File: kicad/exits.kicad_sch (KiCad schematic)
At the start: 54 parts, among them J1 PJ301M12, J12 Euro power header, J13 PJ301M12, J14 PJ301M12, J2 PJ301M12, J3 PJ301M12, J4 PJ301M12, J5 Attenuator Jumper 1, J6 Attenuator Jumper 2, U1 TL074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

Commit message: note about pot taper
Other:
- note added: "Expect input signals to be 10Vpp (i.e +5V to -5V)"
- note added: "While most of the internet says we should use a log (A) pot for volume, I'm copying the Erica Synths Output, Exits, and the Befaco Hexmix, which all used a B10K for volume"
- note removed: "Expect inputs of 5Vpp"
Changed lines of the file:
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@@
     (effects (font (size 1.524 1.524)) (justify left bottom))
   )
-  (text "headphone volume" (at 71.755 156.845 90)
-    (effects (font (size 1.524 1.524)) (justify left bottom))
+  (text "headphone volume" (at 76.2 135.89 180)
+    (effects (font (size 1.524 1.524)) (justify right bottom))
   )
   (text "3.39hz highpass" (at 88.9 121.92 0)
@@
     (effects (font (size 1.524 1.524)) (justify left bottom))
   )
+  (text "While most of the internet says we should use a log (A) pot\nfor volume, I'm copying the Erica Synths Output, Exits,\nand the Befaco Hexmix, which all used a B10K for volume"
+    (at 13.335 152.4 0)
+    (effects (font (size 1.524 1.524)) (justify left bottom))
+  )
   (text "OUTPUTS" (at 89.535 22.225 0)
     (effects (font (size 2.9972 2.9972)) (justify left bottom))
@@
     (effects (font (size 1.524 1.524)) (justify left bottom))
   )
-  (text "Expect inputs of 5Vpp" (at 19.685 19.685 0)
+  (text "Expect input signals to be\n10Vpp (i.e +5V to -5V)" (at 18.415 19.685 0)
     (effects (font (size 1.524 1.524)) (justify left bottom))
   )
@@
   )
   (text "Resistance is highest between\n - pot pins 1 and 2 when the pot is turned fully CCW\n - pot pins 3 and 2 when the pot is turned fully CW\n\nFor a volume voltage divider (CCW = quiet, CW = loud)\n - signal is on pin 1\n - output on pin 2\n - pin 3 is gnd\n\nFor a resistive panning pot (signal comes in on pin 2)\n - turning CCW lowers the level on pin 1 - so 1 is R\n - turning CW lowers the level on pin 3 - so 3 is L\n"
-    (at 12.7 196.85 0)
+    (at 12.7 196.215 0)
     (effects (font (size 1.524 1.524)) (justify left bottom))
   )

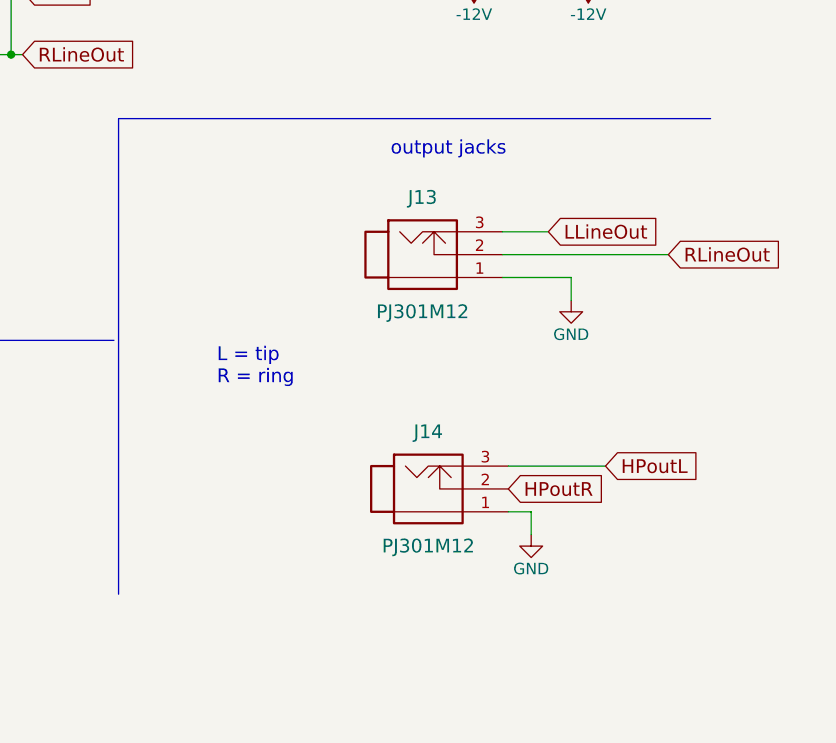
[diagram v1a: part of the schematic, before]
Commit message: switch to PJ358s for stereo output
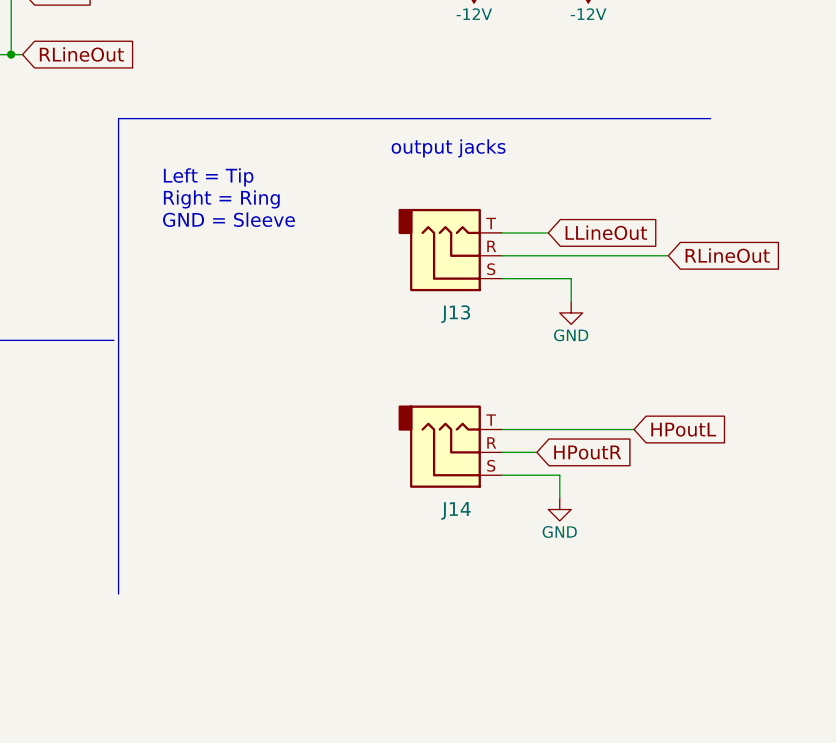
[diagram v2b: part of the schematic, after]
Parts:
- J13, J14: value PJ301M12 -> (none); footprint nearness:PJ301M12 -> (none); symbol pj301m12:PJ301M12 -> Connector:AudioJack3
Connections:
- net GND: now also J13.S, J14.S; no longer J13.1, J14.1
- net HPoutL: now also J14.T; no longer J14.3
- net HPoutR: now also J14.R; no longer J14.2
- net LLineOut: now also J13.T; no longer J13.3
- net RLineOut: now also J13.R; no longer J13.2
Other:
- note added: "Left = Tip Right = Ring GND = Sleeve"
- note removed: "L = tip R = ring"

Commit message: switch to PJ341s, add linearizing Rs
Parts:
- added R2, R4: LIN1.5K, Resistor_THT:R_Axial_DIN0207_L6.3mm_D2.5mm_P2.54mm_Vertical, symbol Device:R
- C1, C2: footprint Capacitor_SMD:C_1206_3216Metric -> Capacitor_SMD:C_1206_3216Metric_Pad1.33x1.80mm_HandSolder
- C10, C7, C8, C9: footprint Capacitor_SMD:C_0603_1608Metric -> Capacitor_SMD:C_0603_1608Metric_Pad1.08x0.95mm_HandSolder
- C5, C6: footprint Capacitor_SMD:C_0805_2012Metric -> Capacitor_SMD:C_0805_2012Metric_Pad1.18x1.45mm_HandSolder
- J1, J2, J3, J4: value PJ301M12 -> PJ341; footprint nearness:PJ301M12 -> nearness:PJ341; symbol pj301m12:PJ301M12 -> Connector:AudioJack3
- J13, J14: value (none) -> PJ341; footprint (none) -> nearness:PJ341
- R1, R17, R19, R20, R21, R22, R27, R28, R29, R3, R30, R38, R5, R7: footprint Resistor_SMD:R_0603_1608Metric -> Resistor_SMD:R_0603_1608Metric_Pad0.98x0.95mm_HandSolder
- R15, R16, R35, R36: footprint Resistor_SMD:R_0805_2012Metric -> Resistor_SMD:R_0805_2012Metric_Pad1.20x1.40mm_HandSolder
- R23, R24, R25, R26: footprint Resistor_SMD:R_0805_2012Metric -> Resistor_SMD:R_0603_1608Metric_Pad0.98x0.95mm_HandSolder
- R33, R34: footprint Resistor_SMD:R_1206_3216Metric -> Resistor_SMD:R_1206_3216Metric_Pad1.30x1.75mm_HandSolder
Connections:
- net GND: now also J1.R, J1.S, J2.R, J2.S, J3.R, J3.S, J4.R, J4.S, R2.2, R4.2; no longer J1.1, J1.2, J2.1, J2.2, J3.1, J3.2, J4.1, J4.2
- net LLineOut: no longer R35.2
- net RLineOut: no longer R36.2
- net Lout: now reaches R27.2, R29.1, U1.1
- net Lout: now also R35.2
- net Rout: now reaches R28.2, R30.1, U1.8
- net Rout: now also R36.2
- net at RV3.1: now also J2.T; no longer J2.3
- net at RV2.1: now also J1.T; no longer J1.3
- net at C2.1, RV1.5: now also R2.1
- net at RV4.1: now also J3.T; no longer J3.3
- net at RV5.1: now also J4.T; no longer J4.3
- net at C1.1, RV1.2: now also R4.1
